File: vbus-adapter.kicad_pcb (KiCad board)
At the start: 2 copper layers, 76.5 x 49 mm, 50 parts, among them J1 VBUS, J2 CAN, J3 Sens 2, J4 Sens 1, J5 Power, J6 Backup GPIO, J7 Program, Q1 SS8050, Q2 SS8050, T800 AO3400A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

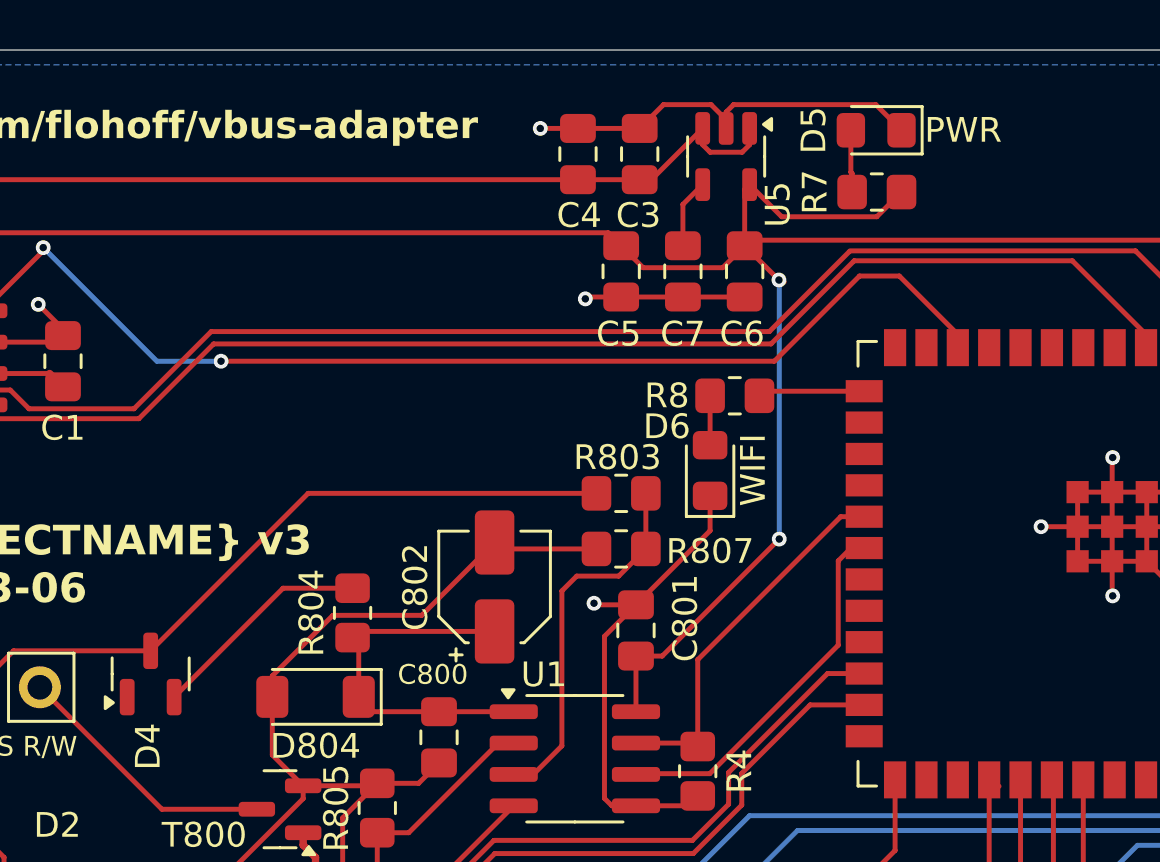
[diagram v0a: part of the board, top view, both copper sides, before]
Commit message: Fix footprint for C802
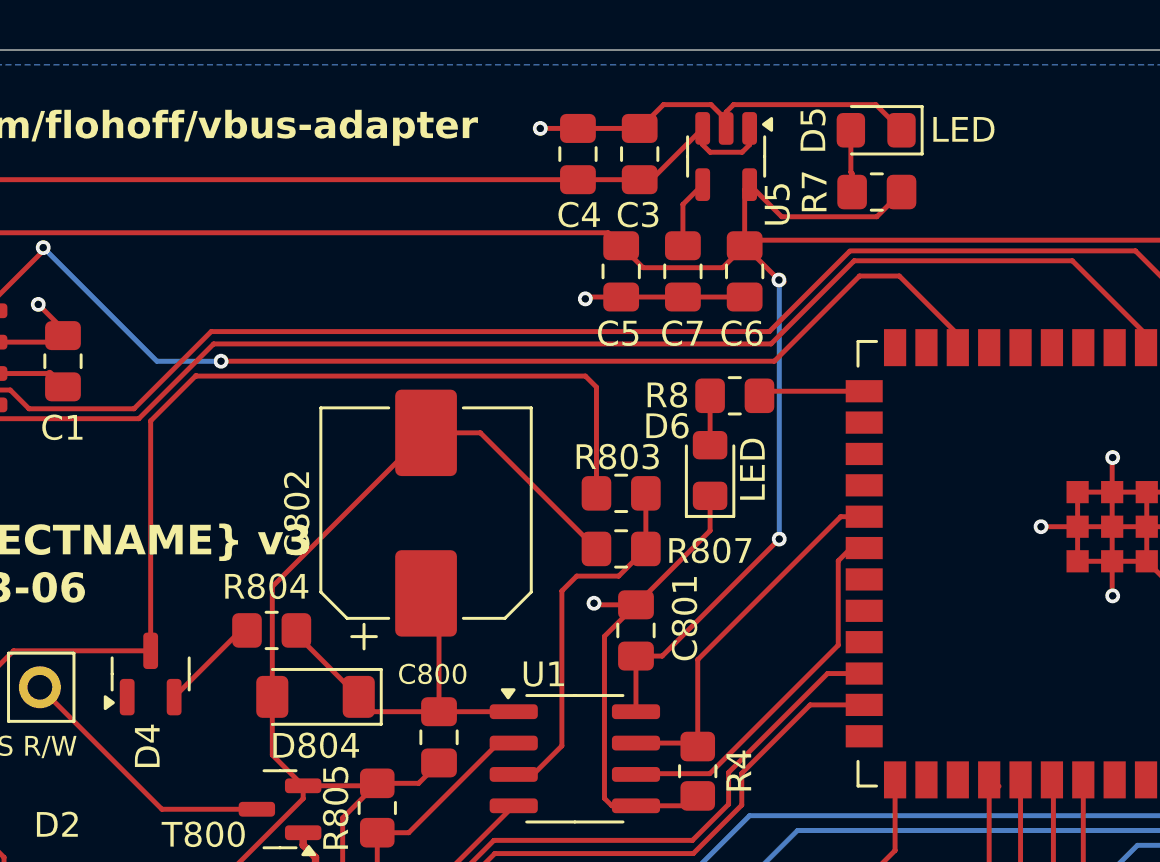
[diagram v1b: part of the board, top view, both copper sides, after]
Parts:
- C802: footprint Capacitor_SMD:CP_Elec_4x3.9 -> Capacitor_SMD:CP_Elec_8x10
- D5: value PWR -> LED
- D6: value WIFI -> LED
- moved C802 4.08 mm to (148.5, 91.8)
- moved R804 3.35 mm to (142.2, 96.5), turned to 180 degrees
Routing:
- net Net-(D2-K): track 36.8 -> 48.7 mm
- net VBUS-GND: track 61.4 -> 67.2 mm
- net Net-(D4-K): track 9.05 -> 4.07 mm

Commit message: Version 4
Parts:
- added C10: 10uF, Capacitor_SMD:C_0805_2012Metric, F.Cu at (170.8, 77.2)
- added C8: 1uF, Capacitor_SMD:C_0805_2012Metric, F.Cu at (176.7, 81.8)
- added C9: 100nF, Capacitor_SMD:C_0805_2012Metric, F.Cu at (173.2, 77.2)
- added R9: 10k, Resistor_SMD:R_0805_2012Metric, F.Cu at (176.7, 79.8)
- C4, C5: value 0.1uF -> 100nF
- D804: value ZMM5V1 -> BZY55B5V1RBG; footprint Diode_SMD:D_MiniMELF -> Diode_SMD:D_0805_2012Metric
- J6: footprint Connector_PinHeader_2.54mm:PinHeader_1x06_P2.54mm_Vertical -> Connector_PinHeader_2.54mm:PinHeader_1x07_P2.54mm_Vertical
- moved J6 2.69 mm to (161.1, 117.3)
- turned C1 to -90 degrees
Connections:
- J6 pad 3: EXT1 -> +5V
- J6 pad 4: EXT2 -> EXT1
- J6 pad 5: EXT3 -> EXT2
- J6 pad 6: EXT4 -> EXT3
- U3 pad 2: +5V -> GND
- U3 pad 3: GND -> +5V
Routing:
- net GND: track 96.4 -> 150.7 mm
- net +5V: track 107.6 -> 156.9 mm
- net EN: track 37.3 -> 45.1 mm
- net VCC: track 178.1 -> 178.8 mm
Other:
- board text added: "GND VCC +5V E1 E2 E3 E4"
- board text removed: "GND VCC E1 E2 E3 E4"

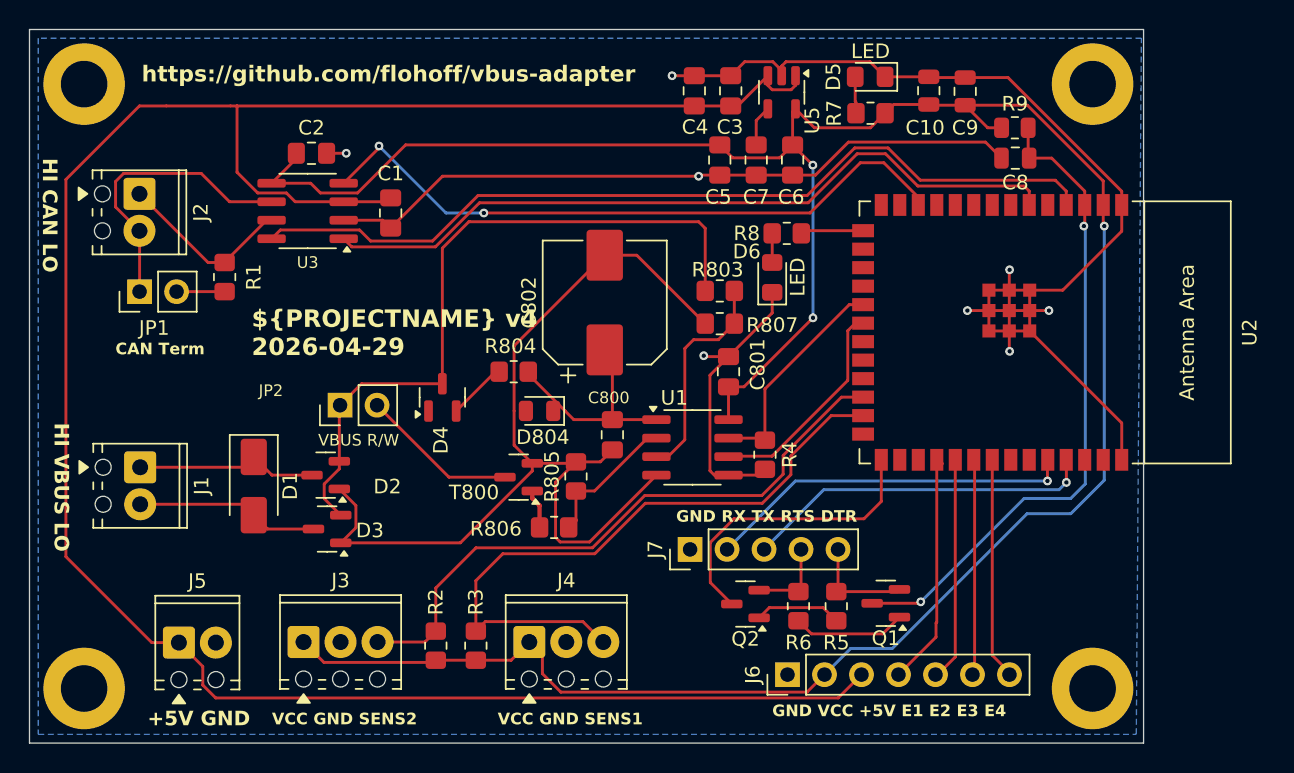
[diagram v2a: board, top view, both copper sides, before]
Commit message: Version 5
- Reposition connectors for Programming
- Add +5V to Sensor Connector
- Make VCC on SENS connector from GPIO
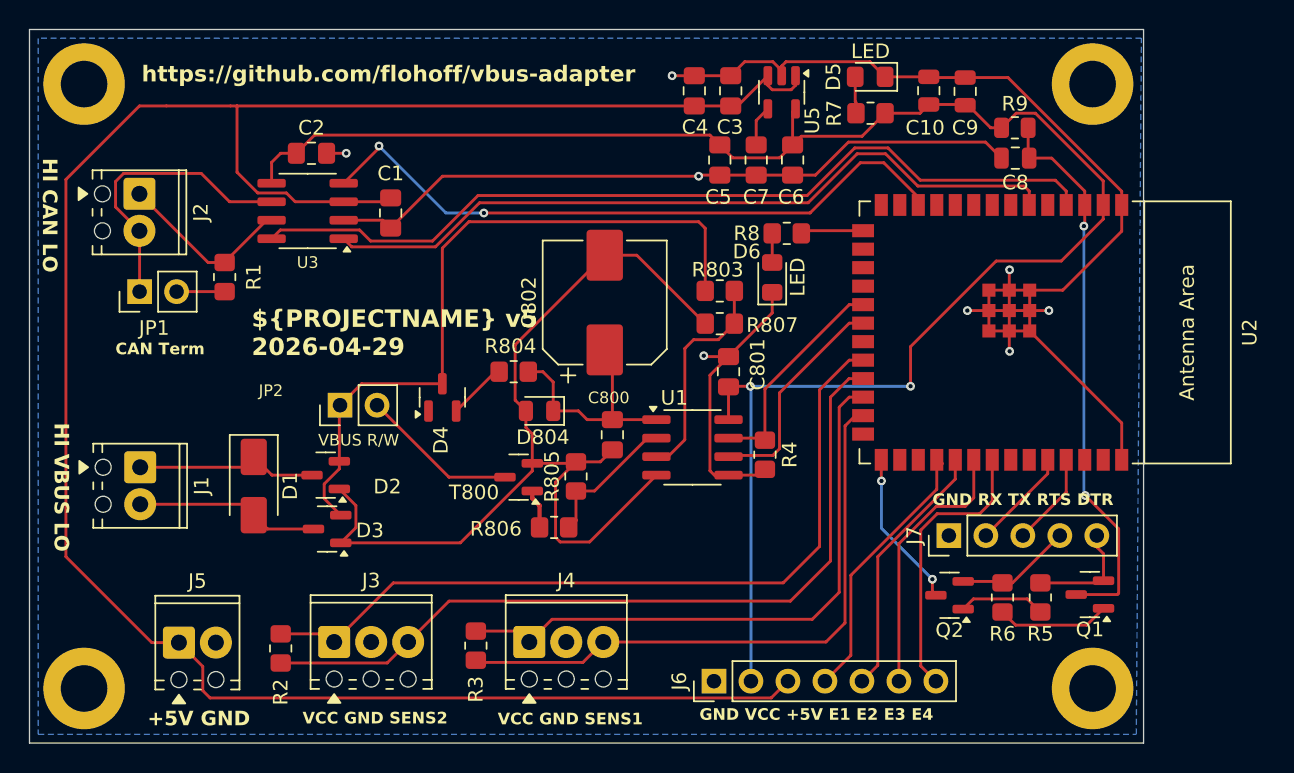
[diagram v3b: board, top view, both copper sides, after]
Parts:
- moved J7 17.8 mm to (172.1, 107.8)
- moved Q2 14.0 mm to (172.2, 111.8)
- moved Q1 14.0 mm to (181.8, 111.8)
- moved R5 14.0 mm to (178.4, 112.0)
- moved R6 14.0 mm to (175.8, 112.0)
- moved R2 10.7 mm to (126.2, 115.5), turned to -90 degrees
- moved J6 5.07 mm to (156.0, 117.8)
- moved J3 2.10 mm to (129.9, 115.1)
- turned R3 to -90 degrees
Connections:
- J3 pad 1: VCC -> PWR-SENS2
- J4 pad 1: VCC -> PWR-SENS1
- R2 pad 1: VCC -> PWR-SENS2
- R3 pad 1: VCC -> PWR-SENS1
- U2 pad 22: unconnected-(U2-GPIO14/TOUCH14/ADC2_CH3/FSPIWP/FSPIDQS-Pad22) -> PWR-SENS2
- U2 pad 23: unconnected-(U2-GPIO21-Pad23) -> GPIO-SENS2
- U2 pad 24: GPIO-SENS2 -> PWR-SENS1
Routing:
- net PWR-SENS2: track 0.00 -> 54.5 mm
- net VCC: track 178.8 -> 124.3 mm, vias 3 -> 2
- net PWR-SENS1: track 0.00 -> 41.3 mm
- net PROG_RXD: track 25.4 -> 6.96 mm, vias 1 -> 0
- net PROG_TXD: track 24.2 -> 6.43 mm, vias 1 -> 0
- net GPIO-SENS2: track 42.8 -> 54.7 mm
- net PROG: track 20.6 -> 10.9 mm, vias 0 -> 2
- net EN: track 45.1 -> 38.4 mm
- net +5V: track 156.9 -> 151.9 mm
- net EXT4: track 15.3 -> 19.4 mm
- net EXT3: track 14.8 -> 18.5 mm
- net GPIO-SENS1: track 45.1 -> 41.6 mm
- net EXT2: track 15.3 -> 17.9 mm
- net EXT1: track 15.9 -> 18.5 mm
- net Net-(J7-Pin_4): track 5.72 -> 8.03 mm
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
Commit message: Small fixes
- Label placement
- Remove redundant PWR_FLAG
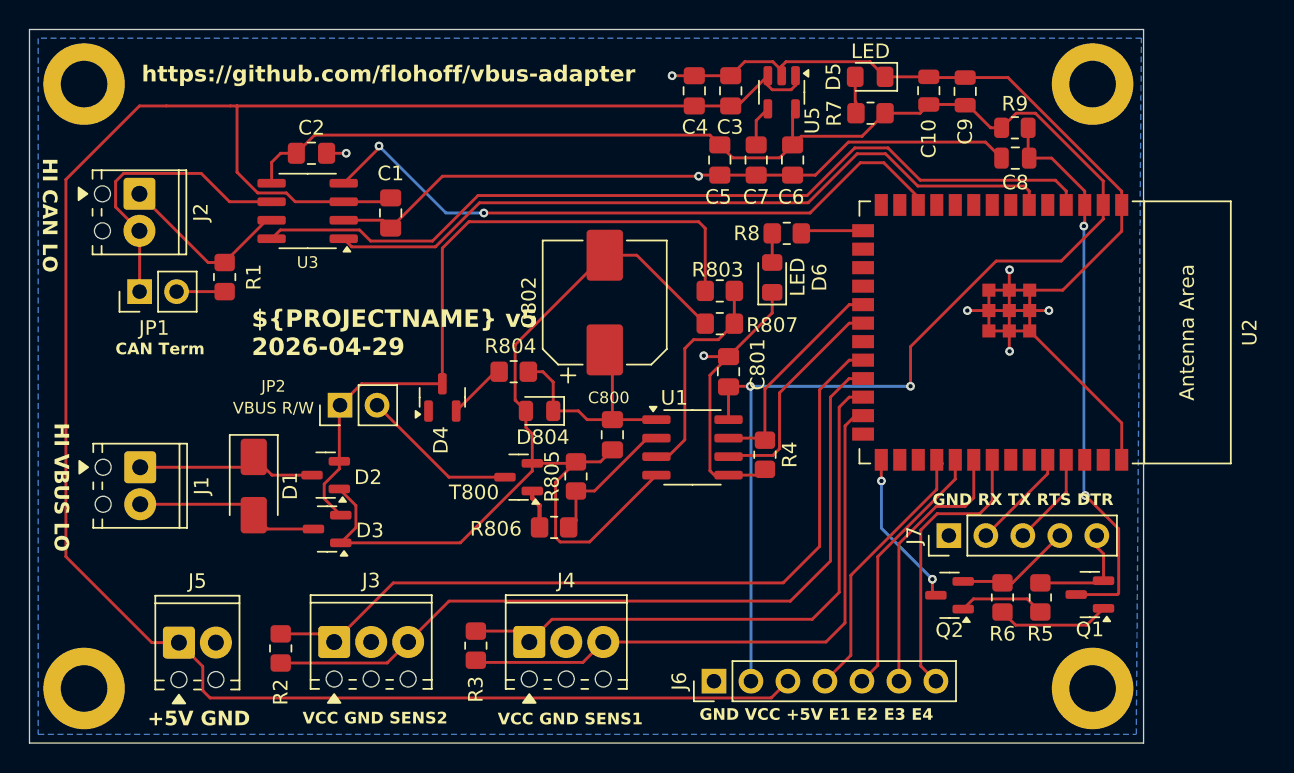
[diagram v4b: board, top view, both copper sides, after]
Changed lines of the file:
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@@
 		(tags "capacitor")
 		(property "Reference" "C10"
-			(at 2.55 0.25 180)
+			(at 3.3 0 90)
 			(layer "F.SilkS")
 			(effects
@@
 		(tags "Through hole pin header THT 1x02 2.54mm single row")
 		(property "Reference" "JP2"
-			(at 1 -4.75 0)
+			(at 1.3 -4.575 0)
 			(layer "F.SilkS")
 			(effects
@@
 		)
 		(property "Value" "VBUS R/W"
-			(at -2.4 1.275 0)
+			(at -0.2 -4.575 0)
 			(layer "F.SilkS")
 			(effects
@@
 		(tags "SOT TO_SOT_SMD")
 		(property "Reference" "D2"
-			(at -4.2375 -0.79 0)
+			(at -2.9125 -0.15 0)
 			(layer "F.SilkS")
 			(effects
@@
 		(tags "LED handsolder")
 		(property "Reference" "D6"
-			(at 1.775 -1.75 180)
+			(at 0 3.25 270)
 			(layer "F.SilkS")
 			(effects
@@
 		(tags "capacitor")
 		(property "Reference" "C9"
-			(at 2.5 0 180)
+			(at 2.75 0 270)
 			(layer "F.SilkS")
 			(effects

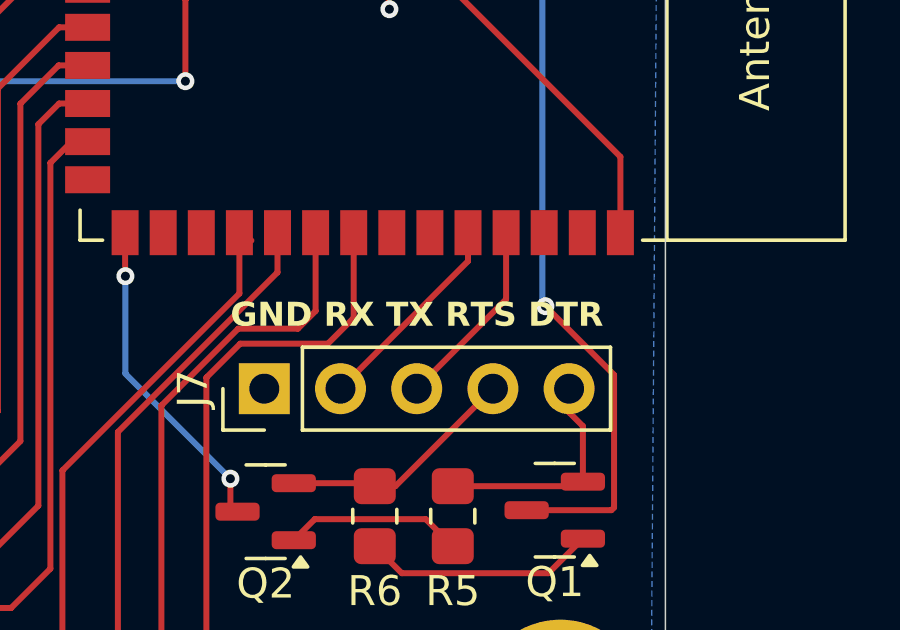
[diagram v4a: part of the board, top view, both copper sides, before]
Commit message: Fix programming adapter Labeling
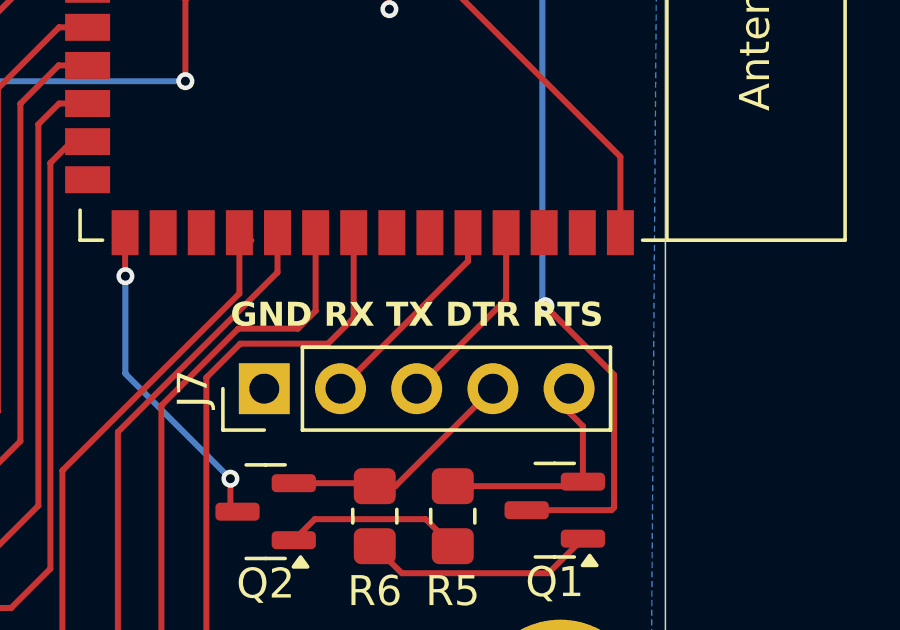
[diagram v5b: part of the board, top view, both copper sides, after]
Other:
- board text added: "GND RX TX DTR RTS"
- board text removed: "GND RX TX RTS DTR"
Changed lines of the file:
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@@
 		)
 	)
-	(gr_text "GND RX TX RTS DTR"
+	(gr_text "GND RX TX DTR RTS\n"
 		(at 171 105.75 0)
 		(layer "F.SilkS")
